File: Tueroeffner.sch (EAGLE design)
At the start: 41 parts, among them IC1 NCP1117ST33T3G, IC3 M25PE20, K2 EC2-12TNU, Q1 2N7002CK, Q2 2N7002CK

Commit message: Clean Up
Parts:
- renumbered TP1 to VC, TP2 to RX, TP3 to TX, TP4 to GN, TP5 to MO, TP6 to MI, TP7 to RS, TP8 to SK
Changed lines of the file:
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@@
 <part name="GND5" library="supply1" deviceset="GND" device=""/>
 <part name="5-12V2" library="SparkFun-Aesthetics" deviceset="VCC" device="" value="VCC-5-12V"/>
-<part name="TP1" library="testpad" deviceset="TP" device="B1,27"/>
-<part name="TP2" library="testpad" deviceset="TP" device="B1,27"/>
-<part name="TP3" library="testpad" deviceset="TP" device="B1,27"/>
-<part name="TP4" library="testpad" deviceset="TP" device="B1,27"/>
-<part name="TP5" library="testpad" deviceset="TP" device="B1,27"/>
-<part name="TP6" library="testpad" deviceset="TP" device="B1,27"/>
-<part name="TP7" library="testpad" deviceset="TP" device="B1,27"/>
-<part name="TP8" library="testpad" deviceset="TP" device="B1,27"/>
+<part name="VC" library="testpad" deviceset="TP" device="B1,27"/>
+<part name="RX" library="testpad" deviceset="TP" device="B1,27"/>
+<part name="TX" library="testpad" deviceset="TP" device="B1,27"/>
+<part name="GN" library="testpad" deviceset="TP" device="B1,27"/>
+<part name="MO" library="testpad" deviceset="TP" device="B1,27"/>
+<part name="MI" library="testpad" deviceset="TP" device="B1,27"/>
+<part name="RS" library="testpad" deviceset="TP" device="B1,27"/>
+<part name="SK" library="testpad" deviceset="TP" device="B1,27"/>
 </parts>
 <sheets>
@@
 <instance part="GND5" gate="1" x="320.04" y="17.78"/>
 <instance part="5-12V2" gate="G$1" x="304.8" y="45.72"/>
-<instance part="TP1" gate="G$1" x="157.48" y="81.28" rot="R270"/>
-<instance part="TP2" gate="G$1" x="157.48" y="78.74" rot="R270"/>
-<instance part="TP3" gate="G$1" x="157.48" y="76.2" rot="R270"/>
-<instance part="TP4" gate="G$1" x="157.48" y="73.66" rot="R270"/>
-<instance part="TP5" gate="G$1" x="167.64" y="78.74" rot="R90"/>
-<instance part="TP6" gate="G$1" x="167.64" y="76.2" rot="R90"/>
-<instance part="TP7" gate="G$1" x="167.64" y="71.12" rot="R90"/>
-<instance part="TP8" gate="G$1" x="167.64" y="73.66" rot="R90"/>
+<instance part="VC" gate="G$1" x="157.48" y="81.28" smashed="yes" rot="R270">
+<attribute name="NAME" x="158.75" y="80.01" size="1.778" layer="95"/>
+<attribute name="TP_SIGNAL_NAME" x="156.21" y="80.01" size="1.778" layer="97" rot="R270"/>
+</instance>
+<instance part="RX" gate="G$1" x="157.48" y="78.74" smashed="yes" rot="R270">
+<attribute name="NAME" x="158.75" y="77.47" size="1.778" layer="95"/>
+<attribute name="TP_SIGNAL_NAME" x="156.21" y="77.47" size="1.778" layer="97" rot="R270"/>
+</instance>
+<instance part="TX" gate="G$1" x="157.48" y="76.2" smashed="yes" rot="R270">
+<attribute name="NAME" x="158.75" y="74.93" size="1.778" layer="95"/>
+<attribute name="TP_SIGNAL_NAME" x="156.21" y="74.93" size="1.778" layer="97" rot="R270"/>
+</instance>
+<instance part="GN" gate="G$1" x="157.48" y="73.66" smashed="yes" rot="R270">
+<attribute name="NAME" x="158.75" y="72.39" size="1.778" layer="95"/>
+<attribute name="TP_SIGNAL_NAME" x="156.21" y="72.39" size="1.778" layer="97" rot="R270"/>
+</instance>
+<instance part="MO" gate="G$1" x="167.64" y="78.74" smashed="yes" rot="R90">
+<attribute name="NAME" x="166.37" y="80.01" size="1.778" layer="95" rot="R180"/>
+<attribute name="TP_SIGNAL_NAME" x="168.91" y="80.01" size="1.778" layer="97" rot="R90"/>
+</instance>
+<instance part="MI" gate="G$1" x="167.64" y="76.2" smashed="yes" rot="R90">
+<attribute name="NAME" x="166.37" y="77.47" size="1.778" layer="95" rot="R180"/>
+<attribute name="TP_SIGNAL_NAME" x="168.91" y="77.47" size="1.778" layer="97" rot="R90"/>
+</instance>
+<instance part="RS" gate="G$1" x="167.64" y="71.12" smashed="yes" rot="R90">
+<attribute name="NAME" x="166.37" y="72.39" size="1.778" layer="95" rot="R180"/>
+<attribute name="TP_SIGNAL_NAME" x="168.91" y="72.39" size="1.778" layer="97" rot="R90"/>
+</instance>
+<instance part="SK" gate="G$1" x="167.64" y="73.66" smashed="yes" rot="R90">
+<attribute name="NAME" x="166.37" y="74.93" size="1.778" layer="95" rot="R180"/>
+<attribute name="TP_SIGNAL_NAME" x="168.91" y="74.93" size="1.778" layer="97" rot="R90"/>
+</instance>
 </instances>
 <busses>
@@
 <wire x1="154.94" y1="73.66" x2="149.86" y2="73.66" width="0.1524" layer="91"/>
 <wire x1="149.86" y1="66.04" x2="149.86" y2="73.66" width="0.1524" layer="91"/>
-<pinref part="TP4" gate="G$1" pin="TP"/>
+<pinref part="GN" gate="G$1" pin="TP"/>
 </segment>
 <segment>
@@
 <wire x1="154.94" y1="81.28" x2="149.86" y2="81.28" width="0.1524" layer="91"/>
 <wire x1="149.86" y1="81.28" x2="149.86" y2="83.82" width="0.1524" layer="91"/>
-<pinref part="TP1" gate="G$1" pin="TP"/>
+<pinref part="VC" gate="G$1" pin="TP"/>
 </segment>
 <segment>
@@
 <segment>
 <label x="149.86" y="76.2" size="0.8128" layer="95" rot="R180" xref="yes"/>
-<pinref part="TP3" gate="G$1" pin="TP"/>
+<pinref part="TX" gate="G$1" pin="TP"/>
 <wire x1="154.94" y1="76.2" x2="149.86" y2="76.2" width="0.1524" layer="91"/>
 </segment>
@@
 <segment>
 <label x="149.86" y="78.74" size="0.8128" layer="95" rot="R180" xref="yes"/>
-<pinref part="TP2" gate="G$1" pin="TP"/>
+<pinref part="RX" gate="G$1" pin="TP"/>
 <wire x1="154.94" y1="78.74" x2="149.86" y2="78.74" width="0.1524" layer="91"/>
 </segment>
@@
 <segment>
 <label x="175.26" y="71.12" size="0.8128" layer="95" ratio="7" xref="yes"/>
-<pinref part="TP7" gate="G$1" pin="TP"/>
+<pinref part="RS" gate="G$1" pin="TP"/>
 <wire x1="170.18" y1="71.12" x2="175.26" y2="71.12" width="0.1524" layer="91"/>
 </segment>
@@
 <segment>
 <label x="175.26" y="78.74" size="0.8128" layer="95" ratio="7" xref="yes"/>
-<pinref part="TP5" gate="G$1" pin="TP"/>
+<pinref part="MO" gate="G$1" pin="TP"/>
 <wire x1="170.18" y1="78.74" x2="175.26" y2="78.74" width="0.1524" layer="91"/>
 </segment>
@@
 <segment>
 <label x="175.26" y="73.66" size="0.8128" layer="95" ratio="7" xref="yes"/>
-<pinref part="TP8" gate="G$1" pin="TP"/>
+<pinref part="SK" gate="G$1" pin="TP"/>
 <wire x1="170.18" y1="73.66" x2="175.26" y2="73.66" width="0.1524" layer="91"/>
 </segment>
@@
 <segment>
 <label x="175.26" y="76.2" size="0.8128" layer="95" ratio="7" xref="yes"/>
-<pinref part="TP6" gate="G$1" pin="TP"/>
+<pinref part="MI" gate="G$1" pin="TP"/>
 <wire x1="170.18" y1="76.2" x2="175.26" y2="76.2" width="0.1524" layer="91"/>
 </segment>

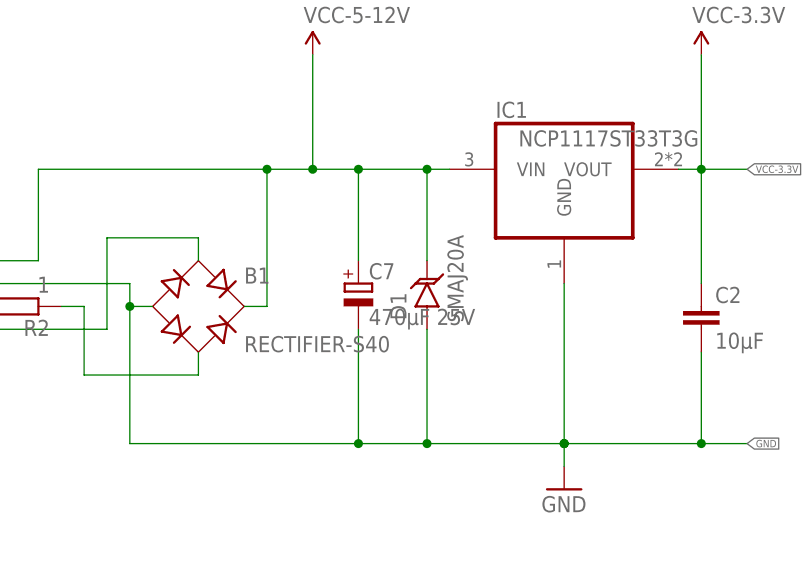
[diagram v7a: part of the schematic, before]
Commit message: little layout changes
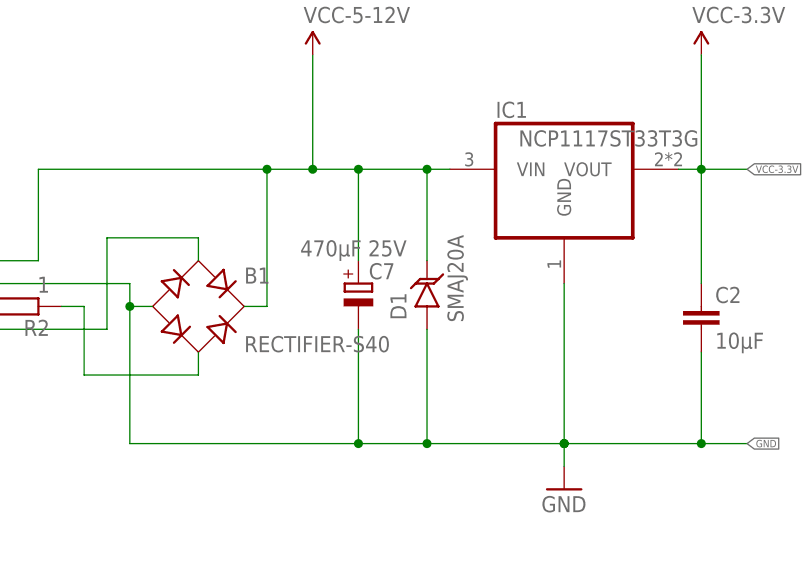
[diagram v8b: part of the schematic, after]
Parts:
- GN, MI, MO, RS, RX, SK, TX, VC: value TPB1,27 -> TPTP14R; device testpad:TPB1,27 -> testpad:TPTP14R
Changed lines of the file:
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@@
 <grid distance="0.1" unitdist="inch" unit="inch" style="lines" multiple="1" display="no" altdistance="0.01" altunitdist="inch" altunit="inch"/>
 <layers>
-<layer number="1" name="Top" color="4" fill="1" visible="no" active="no"/>
-<layer number="2" name="Route2" color="1" fill="3" visible="no" active="no"/>
-<layer number="3" name="Route3" color="4" fill="3" visible="no" active="no"/>
-<layer number="4" name="Route4" color="1" fill="4" visible="no" active="no"/>
-<layer number="5" name="Route5" color="4" fill="4" visible="no" active="no"/>
-<layer number="6" name="Route6" color="1" fill="8" visible="no" active="no"/>
-<layer number="7" name="Route7" color="4" fill="8" visible="no" active="no"/>
-<layer number="8" name="Route8" color="1" fill="2" visible="no" active="no"/>
-<layer number="9" name="Route9" color="4" fill="2" visible="no" active="no"/>
-<layer number="10" name="Route10" color="1" fill="7" visible="no" active="no"/>
-<layer number="11" name="Route11" color="4" fill="7" visible="no" active="no"/>
-<layer number="12" name="Route12" color="1" fill="5" visible="no" active="no"/>
-<layer number="13" name="Route13" color="4" fill="5" visible="no" active="no"/>
-<layer number="14" name="Route14" color="1" fill="6" visible="no" active="no"/>
-<layer number="15" name="Route15" color="4" fill="6" visible="no" active="no"/>
-<layer number="16" name="Bottom" color="1" fill="1" visible="no" active="no"/>
-<layer number="17" name="Pads" color="2" fill="1" visible="no" active="no"/>
-<layer number="18" name="Vias" color="2" fill="1" visible="no" active="no"/>
-<layer number="19" name="Unrouted" color="6" fill="1" visible="no" active="no"/>
-<layer number="20" name="Dimension" color="15" fill="1" visible="no" active="no"/>
-<layer number="21" name="tPlace" color="7" fill="1" visible="no" active="no"/>
-<layer number="22" name="bPlace" color="7" fill="1" visible="no" active="no"/>
-<layer number="23" name="tOrigins" color="15" fill="1" visible="no" active="no"/>
-<layer number="24" name="bOrigins" color="15" fill="1" visible="no" active="no"/>
-<layer number="25" name="tNames" color="7" fill="1" visible="no" active="no"/>
-<layer number="26" name="bNames" color="7" fill="1" visible="no" active="no"/>
-<layer number="27" name="tValues" color="7" fill="1" visible="no" active="no"/>
-<layer number="28" name="bValues" color="7" fill="1" visible="no" active="no"/>
+<layer number="1" name="Top" color="4" fill="1" visible="yes" active="no"/>
+<layer number="2" name="Route2" color="1" fill="3" visible="yes" active="no"/>
+<layer number="3" name="Route3" color="4" fill="3" visible="yes" active="no"/>
+<layer number="4" name="Route4" color="1" fill="4" visible="yes" active="no"/>
+<layer number="5" name="Route5" color="4" fill="4" visible="yes" active="no"/>
+<layer number="6" name="Route6" color="1" fill="8" visible="yes" active="no"/>
+<layer number="7" name="Route7" color="4" fill="8" visible="yes" active="no"/>
+<layer number="8" name="Route8" color="1" fill="2" visible="yes" active="no"/>
+<layer number="9" name="Route9" color="4" fill="2" visible="yes" active="no"/>
+<layer number="10" name="Route10" color="1" fill="7" visible="yes" active="no"/>
+<layer number="11" name="Route11" color="4" fill="7" visible="yes" active="no"/>
+<layer number="12" name="Route12" color="1" fill="5" visible="yes" active="no"/>
+<layer number="13" name="Route13" color="4" fill="5" visible="yes" active="no"/>
+<layer number="14" name="Route14" color="1" fill="6" visible="yes" active="no"/>
+<layer number="15" name="Route15" color="4" fill="6" visible="yes" active="no"/>
+<layer number="16" name="Bottom" color="1" fill="1" visible="yes" active="no"/>
+<layer number="17" name="Pads" color="2" fill="1" visible="yes" active="no"/>
+<layer number="18" name="Vias" color="2" fill="1" visible="yes" active="no"/>
+<layer number="19" name="Unrouted" color="6" fill="1" visible="yes" active="no"/>
+<layer number="20" name="Dimension" color="15" fill="1" visible="yes" active="no"/>
+<layer number="21" name="tPlace" color="7" fill="1" visible="yes" active="no"/>
+<layer number="22" name="bPlace" color="7" fill="1" visible="yes" active="no"/>
+<layer number="23" name="tOrigins" color="15" fill="1" visible="yes" active="no"/>
+<layer number="24" name="bOrigins" color="15" fill="1" visible="yes" active="no"/>
+<layer number="25" name="tNames" color="7" fill="1" visible="yes" active="no"/>
+<layer number="26" name="bNames" color="7" fill="1" visible="yes" active="no"/>
+<layer number="27" name="tValues" color="7" fill="1" visible="yes" active="no"/>
+<layer number="28" name="bValues" color="7" fill="1" visible="yes" active="no"/>
 <layer number="29" name="tStop" color="7" fill="3" visible="no" active="no"/>
 <layer number="30" name="bStop" color="7" fill="6" visible="no" active="no"/>
@@
 <layer number="35" name="tGlue" color="7" fill="4" visible="no" active="no"/>
 <layer number="36" name="bGlue" color="7" fill="5" visible="no" active="no"/>
-<layer number="37" name="tTest" color="7" fill="1" visible="no" active="no"/>
-<layer number="38" name="bTest" color="7" fill="1" visible="no" active="no"/>
+<layer number="37" name="tTest" color="7" fill="1" visible="yes" active="no"/>
+<layer number="38" name="bTest" color="7" fill="1" visible="yes" active="no"/>
 <layer number="39" name="tKeepout" color="4" fill="11" visible="no" active="no"/>
 <layer number="40" name="bKeepout" color="1" fill="11" visible="no" active="no"/>
@@
 <layer number="44" name="Drills" color="7" fill="1" visible="no" active="no"/>
 <layer number="45" name="Holes" color="7" fill="1" visible="no" active="no"/>
-<layer number="46" name="Milling" color="3" fill="1" visible="no" active="no"/>
-<layer number="47" name="Measures" color="7" fill="1" visible="no" active="no"/>
-<layer number="48" name="Document" color="7" fill="1" visible="no" active="no"/>
-<layer number="49" name="Reference" color="7" fill="1" visible="no" active="no"/>
-<layer number="50" name="dxf" color="7" fill="1" visible="no" active="no"/>
-<layer number="51" name="tDocu" color="7" fill="1" visible="no" active="no"/>
-<layer number="52" name="bDocu" color="7" fill="1" visible="no" active="no"/>
-<layer number="53" name="tGND_GNDA" color="7" fill="1" visible="no" active="no"/>
-<layer number="54" name="bGND_GNDA" color="7" fill="1" visible="no" active="no"/>
-<layer number="56" name="wert" color="7" fill="1" visible="no" active="no"/>
-<layer number="57" name="tCAD" color="7" fill="1" visible="no" active="no"/>
-<layer number="59" name="tCarbon" color="7" fill="1" visible="no" active="no"/>
-<layer number="60" name="bCarbon" color="7" fill="1" visible="no" active="no"/>
+<layer number="46" name="Milling" color="3" fill="1" visible="yes" active="no"/>
+<layer number="47" name="Measures" color="7" fill="1" visible="yes" active="no"/>
+<layer number="48" name="Document" color="7" fill="1" visible="yes" active="no"/>
+<layer number="49" name="Reference" color="7" fill="1" visible="yes" active="no"/>
+<layer number="50" name="dxf" color="7" fill="1" visible="yes" active="no"/>
+<layer number="51" name="tDocu" color="7" fill="1" visible="yes" active="no"/>
+<layer number="52" name="bDocu" color="7" fill="1" visible="yes" active="no"/>
+<layer number="53" name="tGND_GNDA" color="7" fill="1" visible="yes" active="no"/>
+<layer number="54" name="bGND_GNDA" color="7" fill="1" visible="yes" active="no"/>
+<layer number="56" name="wert" color="7" fill="1" visible="yes" active="no"/>
+<layer number="57" name="tCAD" color="7" fill="1" visible="yes" active="no"/>
+<layer number="59" name="tCarbon" color="7" fill="1" visible="yes" active="no"/>
+<layer number="60" name="bCarbon" color="7" fill="1" visible="yes" active="no"/>
 <layer number="90" name="Modules" color="5" fill="1" visible="yes" active="yes"/>
 <layer number="91" name="Nets" color="2" fill="1" visible="yes" active="yes"/>
@@
 <part name="GND5" library="supply1" deviceset="GND" device=""/>
 <part name="5-12V2" library="SparkFun-Aesthetics" deviceset="VCC" device="" value="VCC-5-12V"/>
-<part name="VC" library="testpad" deviceset="TP" device="B1,27"/>
-<part name="RX" library="testpad" deviceset="TP" device="B1,27"/>
-<part name="TX" library="testpad" deviceset="TP" device="B1,27"/>
-<part name="GN" library="testpad" deviceset="TP" device="B1,27"/>
-<part name="MO" library="testpad" deviceset="TP" device="B1,27"/>
-<part name="MI" library="testpad" deviceset="TP" device="B1,27"/>
-<part name="RS" library="testpad" deviceset="TP" device="B1,27"/>
-<part name="SK" library="testpad" deviceset="TP" device="B1,27"/>
+<part name="VC" library="testpad" deviceset="TP" device="TP14R" value="TPTP14R"/>
+<part name="RX" library="testpad" deviceset="TP" device="TP14R" value="TPTP14R"/>
+<part name="TX" library="testpad" deviceset="TP" device="TP14R" value="TPTP14R"/>
+<part name="GN" library="testpad" deviceset="TP" device="TP14R" value="TPTP14R"/>
+<part name="MO" library="testpad" deviceset="TP" device="TP14R" value="TPTP14R"/>
+<part name="MI" library="testpad" deviceset="TP" device="TP14R" value="TPTP14R"/>
+<part name="RS" library="testpad" deviceset="TP" device="TP14R" value="TPTP14R"/>
+<part name="SK" library="testpad" deviceset="TP" device="TP14R" value="TPTP14R"/>
 </parts>
 <sheets>
@@
 </instance>
 <instance part="B1" gate="G$1" x="30.48" y="22.86"/>
-<instance part="C7" gate="G$1" x="48.26" y="25.4"/>
+<instance part="C7" gate="G$1" x="48.26" y="25.4" smashed="yes">
+<attribute name="NAME" x="49.403" y="25.8826" size="1.778" layer="95"/>
+<attribute name="VALUE" x="41.783" y="28.4226" size="1.778" layer="96"/>
+</instance>
 <instance part="JP2" gate="G$1" x="-2.54" y="22.86"/>
 <instance part="JP3" gate="G$1" x="353.06" y="33.02" rot="R180"/>
